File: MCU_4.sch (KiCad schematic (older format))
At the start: 18 parts, among them U2 STM32F051K6Ux

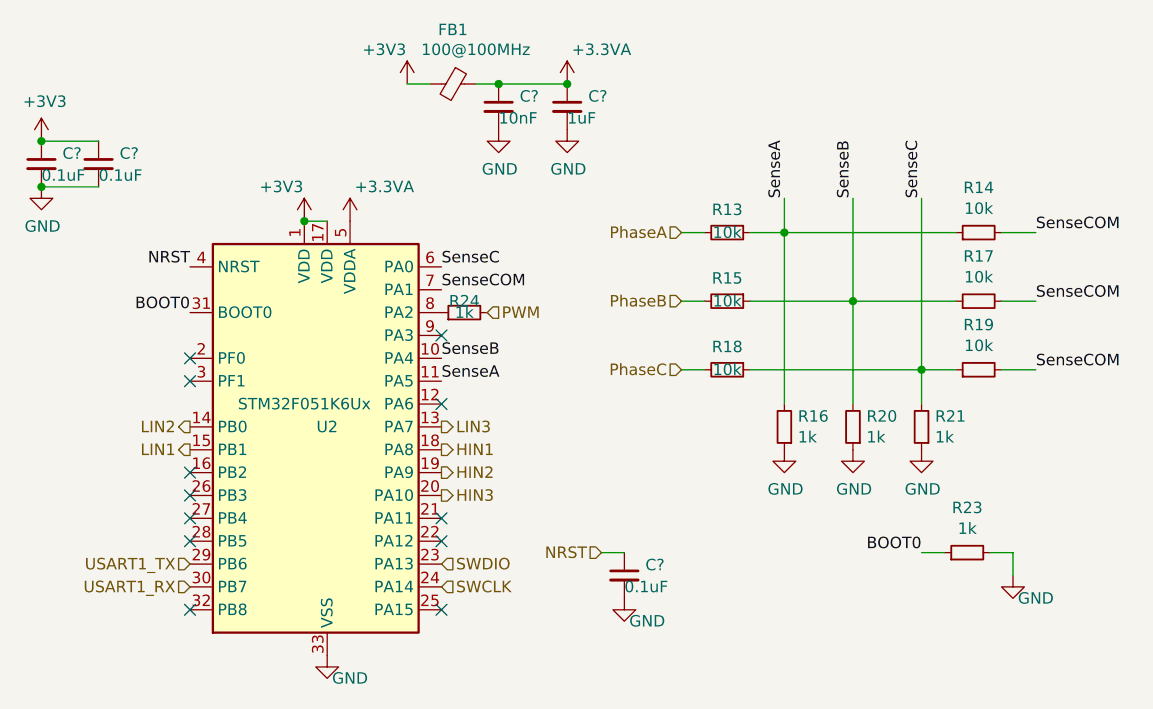
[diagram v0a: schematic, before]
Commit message: Added the rest of the phases and their associated components
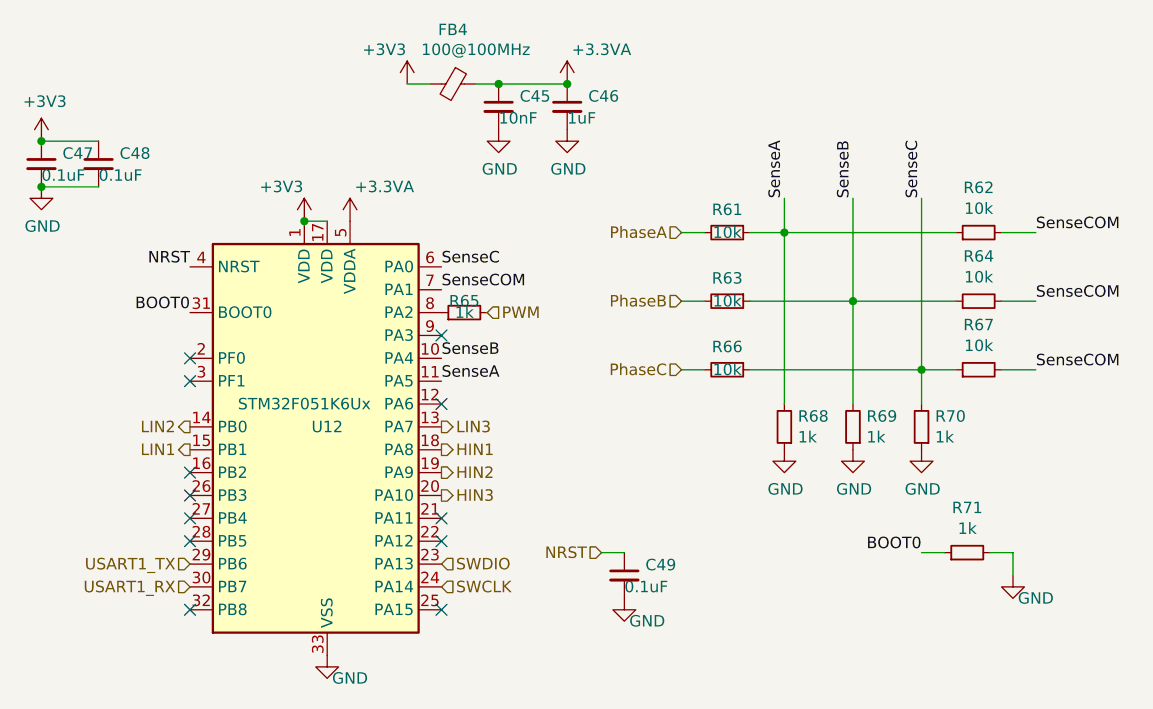
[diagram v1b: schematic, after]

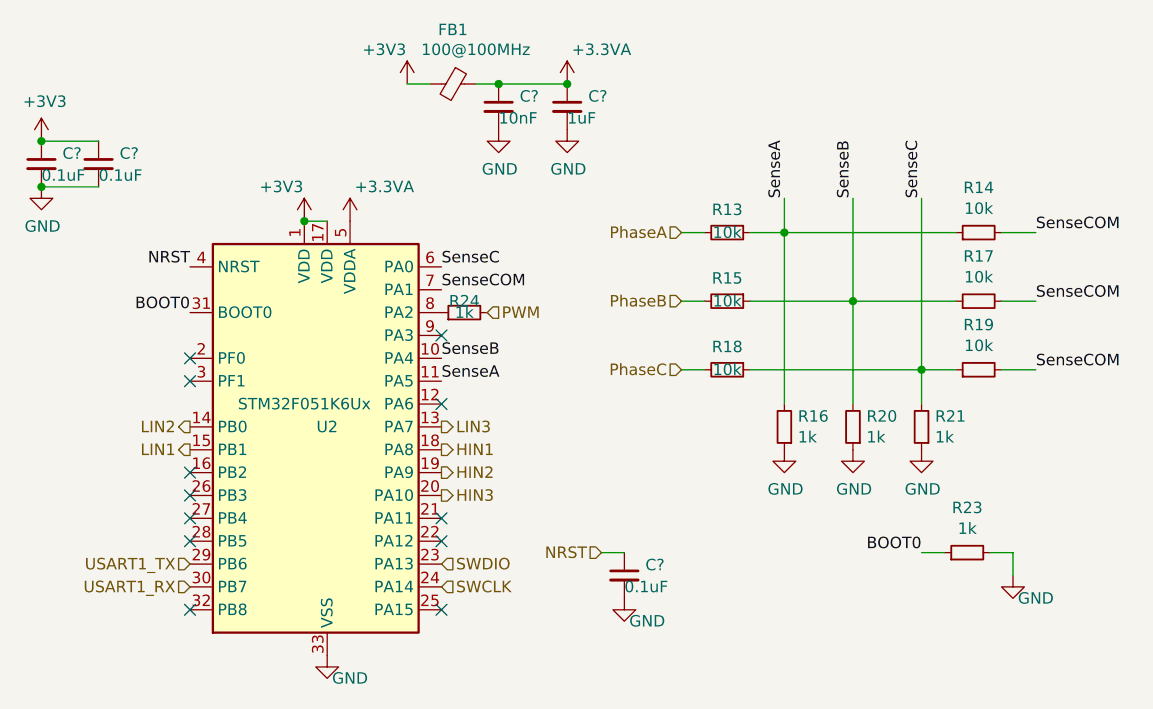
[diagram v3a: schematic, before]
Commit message: Finalized back layer and added FETs to front layer
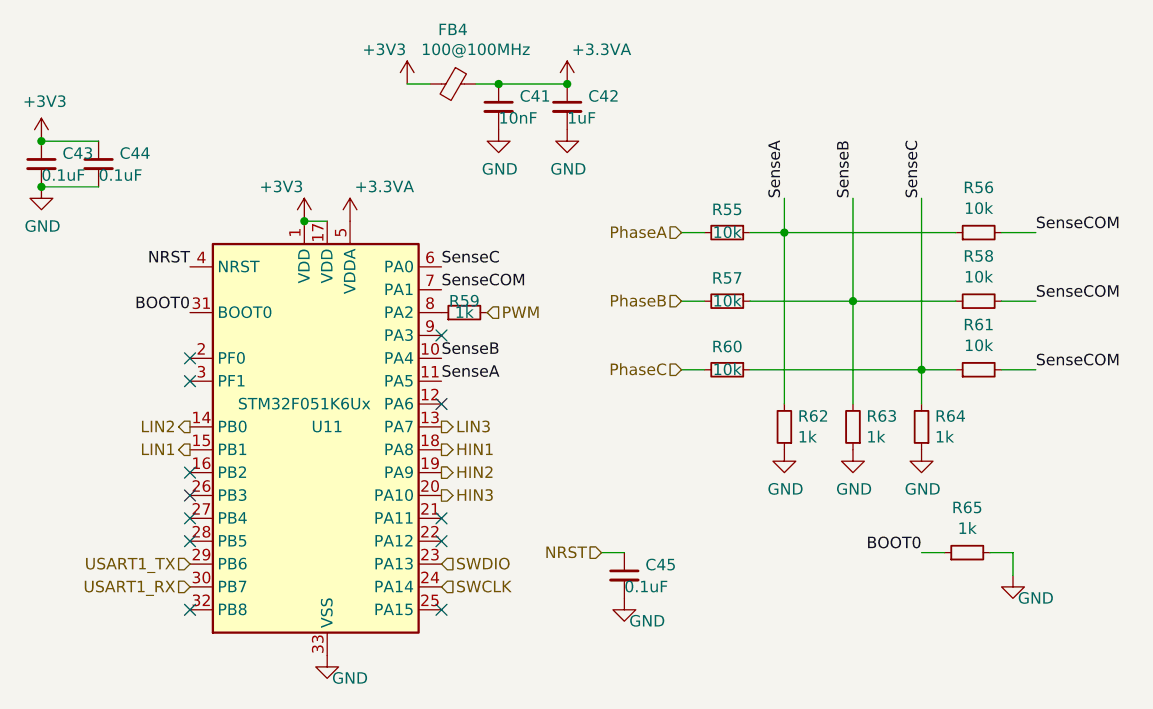
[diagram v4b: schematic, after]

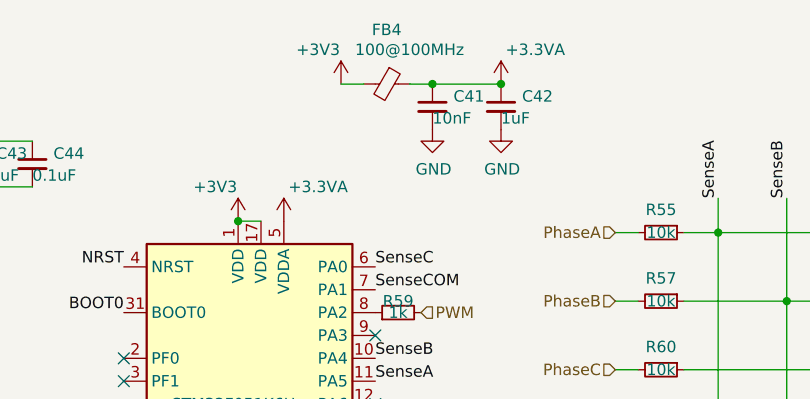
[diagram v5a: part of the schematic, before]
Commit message: Finished all traces and vias
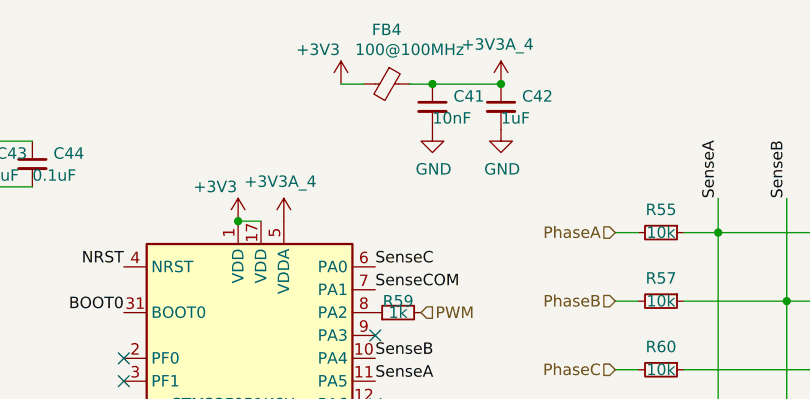
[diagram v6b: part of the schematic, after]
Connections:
- net +3.3VA renamed +3.3VA_4
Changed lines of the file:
@@
 NRST
-$Comp
-L power:+3.3VA #PWR0109
-U 1 1 605D8EC9
-P 5150 2050
-AR Path="/60302A40/605D8EC9" Ref="#PWR0109"  Part="1"
-AR Path="/605793E5/605D8EC9" Ref="#PWR0156"  Part="1"
-AR Path="/6057AB62/605D8EC9" Ref="#PWR?"  Part="1"
-AR Path="/60597D10/605D8EC9" Ref="#PWR0210"  Part="1"
-AR Path="/60653AC5/605D8EC9" Ref="#PWR?"  Part="1"
-AR Path="/60575054/605D8EC9" Ref="#PWR0229"  Part="1"
-AR Path="/605A2EB9/605D8EC9" Ref="#PWR0229"  Part="1"
-AR Path="/6055186B/605D8EC9" Ref="#PWR0214"  Part="1"
-F 0 "#PWR0214" H 5150 1900 50  0001 C CNN
-F 1 "+3.3VA" H 5300 2200 50  0000 C CNN
-F 2 "" H 5150 2050 50  0001 C CNN
-F 3 "" H 5150 2050 50  0001 C CNN
-	1    5150 2050
-	1    0    0    -1
-$EndComp
 $Comp
 L power:+3V3 #PWR0110
@@
 F 3 "" H 5400 1450 50  0001 C CNN
 	1    5400 1450
-	1    0    0    -1
-$EndComp
-$Comp
-L power:+3.3VA #PWR0111
-U 1 1 6059DC36
-P 6100 1450
-AR Path="/60302A40/6059DC36" Ref="#PWR0111"  Part="1"
-AR Path="/605793E5/6059DC36" Ref="#PWR0158"  Part="1"
-AR Path="/6057AB62/6059DC36" Ref="#PWR?"  Part="1"
-AR Path="/60597D10/6059DC36" Ref="#PWR0212"  Part="1"
-AR Path="/60653AC5/6059DC36" Ref="#PWR?"  Part="1"
-AR Path="/60575054/6059DC36" Ref="#PWR0231"  Part="1"
-AR Path="/605A2EB9/6059DC36" Ref="#PWR0231"  Part="1"
-AR Path="/6055186B/6059DC36" Ref="#PWR0220"  Part="1"
-F 0 "#PWR0220" H 6100 1300 50  0001 C CNN
-F 1 "+3.3VA" H 6250 1600 50  0000 C CNN
-F 2 "" H 6100 1450 50  0001 C CNN
-F 3 "" H 6100 1450 50  0001 C CNN
-	1    6100 1450
 	1    0    0    -1
 $EndComp
@@
 Wire Wire Line
 	5700 1450 5800 1450
-Connection ~ 6100 1450
 Wire Wire Line
 	5800 1450 6100 1450
@@
 Text HLabel 4450 3550 0    50   Input ~ 0
 USART1_TX
+$Comp
+L power:+3V3A_4 #PWR0187
+U 1 1 60569D40
+P 5150 2050
+F 0 "#PWR0187" H 5150 2000 50  0001 C CNN
+F 1 "+3V3A_4" H 5135 2223 50  0000 C CNN
+F 2 "" H 5150 2050 50  0001 C CNN
+F 3 "" H 5150 2050 50  0001 C CNN
+	1    5150 2050
+	1    0    0    -1
+$EndComp
+$Comp
+L power:+3V3A_4 #PWR?
+U 1 1 6056B248
+P 6100 1450
+F 0 "#PWR?" H 6100 1400 50  0001 C CNN
+F 1 "+3V3A_4" H 6085 1623 50  0000 C CNN
+F 2 "" H 6100 1450 50  0001 C CNN
+F 3 "" H 6100 1450 50  0001 C CNN
+	1    6100 1450
+	1    0    0    -1
+$EndComp
+Connection ~ 6100 1450
 $EndSCHEMATC
